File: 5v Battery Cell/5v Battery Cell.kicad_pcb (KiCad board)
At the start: 4 copper layers, 42 x 42 mm, 39 parts, among them J1 Conn_01x02_Pin, J2 Conn_01x03_Pin, U1 TPS61023, U2 ATtiny204-SS, U3 MAX17048

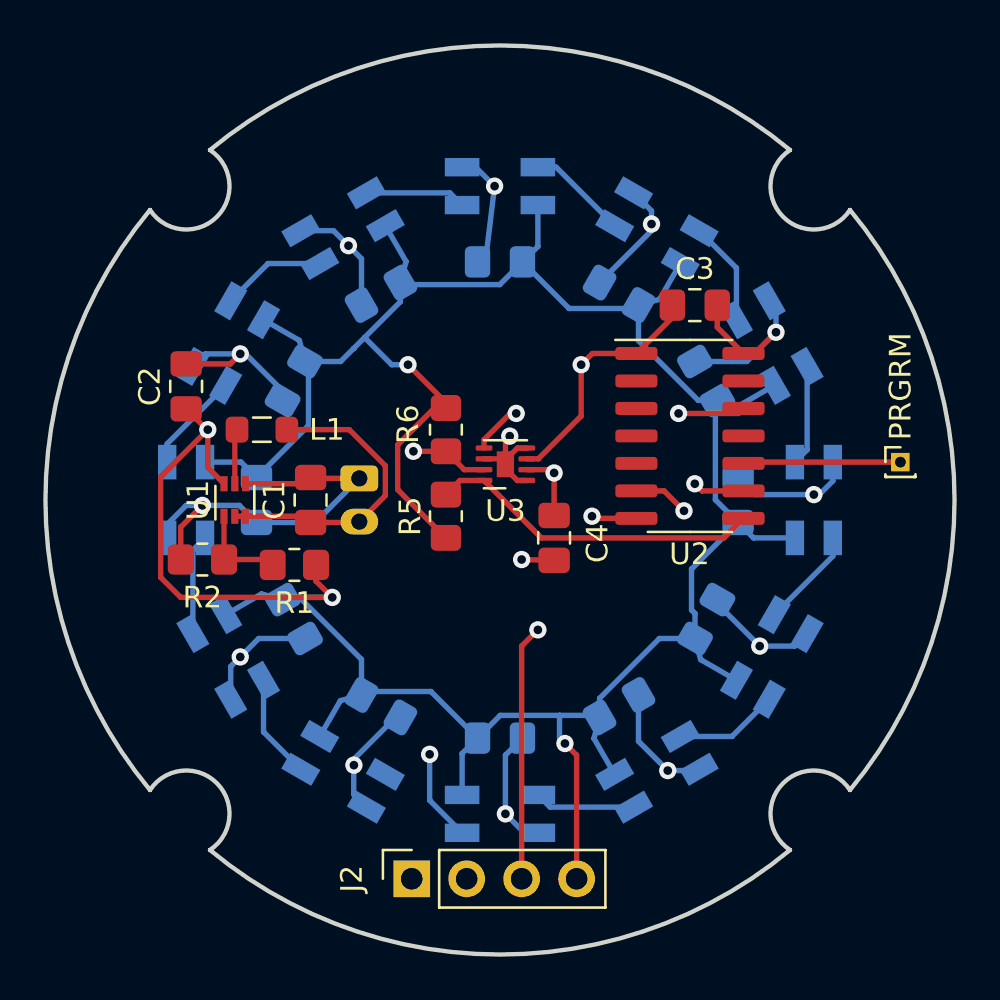
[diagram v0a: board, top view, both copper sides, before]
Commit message: Major revisions to the circuit and PCB design.
Swapped out the ATTiny204 for the AVR16DD14. Gives me extra room to work with. Updated PCB to actually be able to handle 1.5A draw from the battery, though it's never expected to reach that.
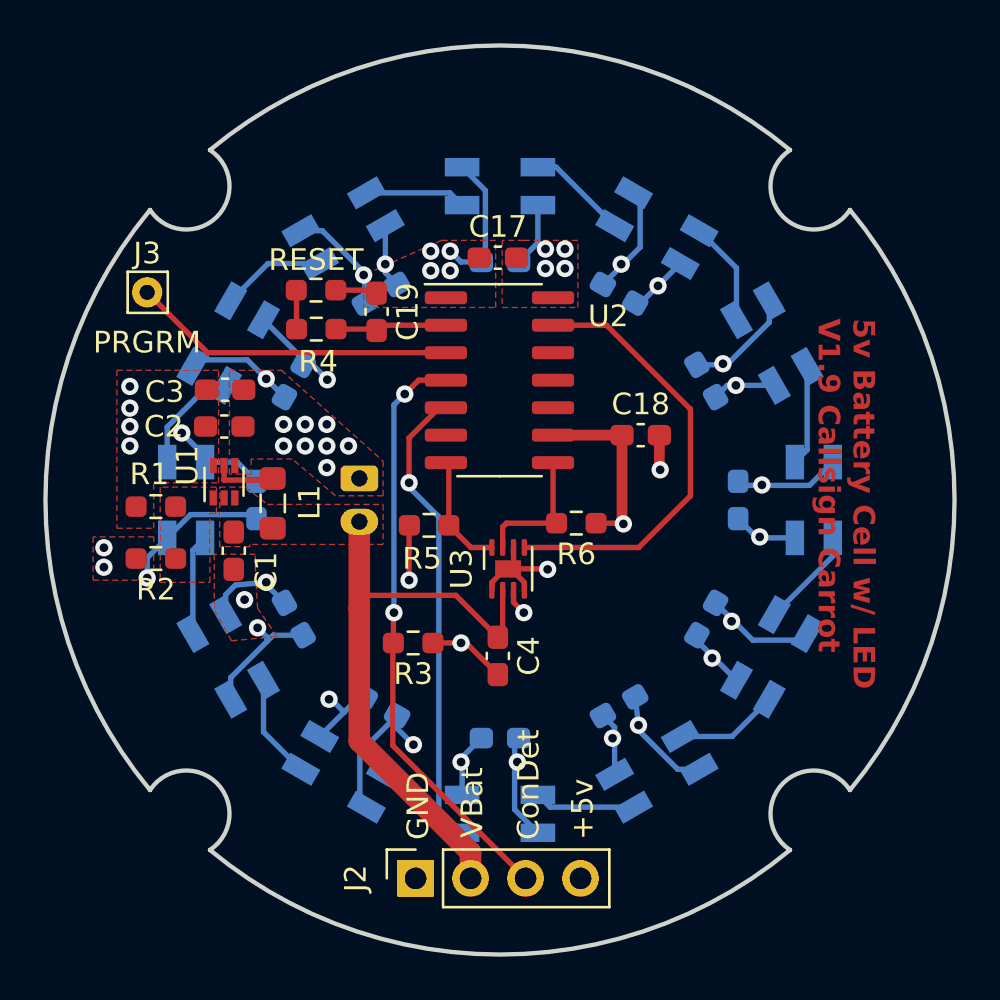
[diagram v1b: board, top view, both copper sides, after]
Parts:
- removed PRGRM: PinHeader_1x01_P1.00mm_Vertical, Connector_PinHeader_1.00mm:PinHeader_1x01_P1.00mm_Vertical
- added C17: 0.1 uF, Capacitor_SMD:C_0603_1608Metric_Pad1.08x0.95mm_HandSolder, F.Cu at (149.4, 87.8)
- added C18: 0.1 uF, Capacitor_SMD:C_0603_1608Metric_Pad1.08x0.95mm_HandSolder, F.Cu at (156.0, 96.0)
- added C19: 0.1 uF, Capacitor_SMD:C_0603_1608Metric_Pad1.08x0.95mm_HandSolder, F.Cu at (143.8, 90.3)
- added J3: PRGRM, Connector_Pin:Pin_D0.7mm_L6.5mm_W1.8mm_FlatFork, F.Cu at (133.2, 89.4)
- added R3: 10k, Resistor_SMD:R_0603_1608Metric_Pad0.98x0.95mm_HandSolder, F.Cu at (145.5, 105.6)
- added R4: 330, Resistor_SMD:R_0603_1608Metric_Pad0.98x0.95mm_HandSolder, F.Cu at (141.0, 91.1)
- added RESET: Reset pad, Resistor_SMD:R_0603_1608Metric_Pad0.98x0.95mm_HandSolder, F.Cu at (141.0, 89.3)
- C1, C10, C11, C12, C13, C14, C15, C16, C2, C3, C4, C5, C6, C7, C8, C9: footprint Capacitor_SMD:C_0805_2012Metric_Pad1.18x1.45mm_HandSolder -> Capacitor_SMD:C_0603_1608Metric_Pad1.08x0.95mm_HandSolder
- R1, R2, R5, R6: footprint Resistor_SMD:R_0805_2012Metric_Pad1.20x1.40mm_HandSolder -> Resistor_SMD:R_0603_1608Metric_Pad0.98x0.95mm_HandSolder
- U2: value ATtiny204-SS -> AVR16DD14
- moved C3 22.0 mm to (136.8, 93.9)
- moved U2 9.17 mm to (149.5, 93.5)
- moved R6 7.41 mm to (153.0, 100.1), turned to 180 degrees
- moved R1 6.94 mm to (133.6, 99.3), turned to 0 degrees
- moved C4 6.04 mm to (149.4, 106.2)
- moved U3 4.84 mm to (149.9, 102.2), turned to 90 degrees
- moved C1 4.25 mm to (137.2, 101.3), turned to -90 degrees
- moved L1 3.44 mm to (139.0, 99.2), turned to 90 degrees
- moved C2 2.56 mm to (136.8, 95.6), turned to 0 degrees
- moved R2 2.15 mm to (133.6, 101.7)
- moved U1 0.98 mm to (136.8, 98.2)
- moved R5 0.88 mm to (146.2, 100.2), turned to 0 degrees
- moved J2 0.18 mm to (145.6, 116.5)
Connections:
- R5 pad 2: /SDA -> SDA
- R6 pad 2: /SCL -> SCL
- U2 pad 1: +5V -> GND
- U2 pad 12: ALRT -> unconnected-(U2-PD6-Pad12)
- U2 pad 13: unconnected-(U2-PA3-Pad13) -> ALRT
- U2 pad 14: GND -> +5V
- U2 pad 2: unconnected-(U2-PA4-Pad2) -> Reset
- U2 pad 3: unconnected-(U2-PA5-Pad3) -> Net-(J3-Pin_1)
- U2 pad 4: unconnected-(U2-PA6-Pad4) -> ConnectDetect
- U2 pad 5: unconnected-(U2-PA7-Pad5) -> LEDControl
- U2 pad 6: LEDControl -> unconnected-(U2-PC1-Pad6)
- U2 pad 7: ConnectDetect -> SDA
- U2 pad 8: /SDA -> SCL
- U2 pad 9: /SCL -> +5V
- U3 pad 7: /SCL -> SCL
- U3 pad 8: /SDA -> SDA
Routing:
- net +5V: track 177.2 -> 52.0 mm, vias 5 -> 22
- net /SCL: track 19.6 -> 0.00 mm, vias 2 -> 0
- net Vbat: track 45.8 -> 28.3 mm, vias 1 -> 0
- net /SDA: track 15.5 -> 0.00 mm
- net Net-(J3-Pin_1): track 0.00 -> 15.0 mm
- net GND: track 89.2 -> 76.9 mm, vias 14 -> 29
- net ALRT: track 13.0 -> 20.6 mm, vias 2 -> 0
- net unconnected-(U2-PD4-Pad10): track 7.19 -> 0.00 mm
- net ConnectDetect: track 20.2 -> 27.3 mm
- net SCL: track 0.00 -> 6.14 mm
- net SDA: track 0.00 -> 5.17 mm
- net Reset: track 0.00 -> 4.97 mm
- net Net-(U1-FB): track 4.00 -> 0.00 mm
- net LEDControl: track 25.0 -> 21.2 mm, vias 2 -> 1
- net Net-(SW1A-B): track 0.00 -> 1.79 mm
- added copper zone on F.Cu, net +5V
- added copper zone on In2.Cu, net +5V
- added copper zone on F.Cu, net GND
- added copper zone on In1.Cu, net GND
- added copper zone on F.Cu, net Net-(U1-FB)
- added copper zone on F.Cu, net Vbat
- removed copper zone on In2.Cu, net GND
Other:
- board text added: "+5v"
- board text added: "5v Battery Cell w/ LED V1.9 Callsign Carrot"
- board text added: "ConDet"
- board text added: "GND"
- board text added: "PRGRM"
- board text added: "VBat"
